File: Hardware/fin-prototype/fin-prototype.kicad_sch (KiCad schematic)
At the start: 80 parts, among them J1 USB_C_Receptacle_USB2.0_16P, J10 Conn_01x01_Pin, J11 Conn_01x01_Pin, J12 Conn_01x01_Pin, J13 Conn_01x01_Pin, J14 Conn_01x01_Pin, J15 Conn_01x01_Pin, J16 Conn_01x01_Pin, J17 Conn_01x01_Pin, J18 Conn_01x01_Pin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

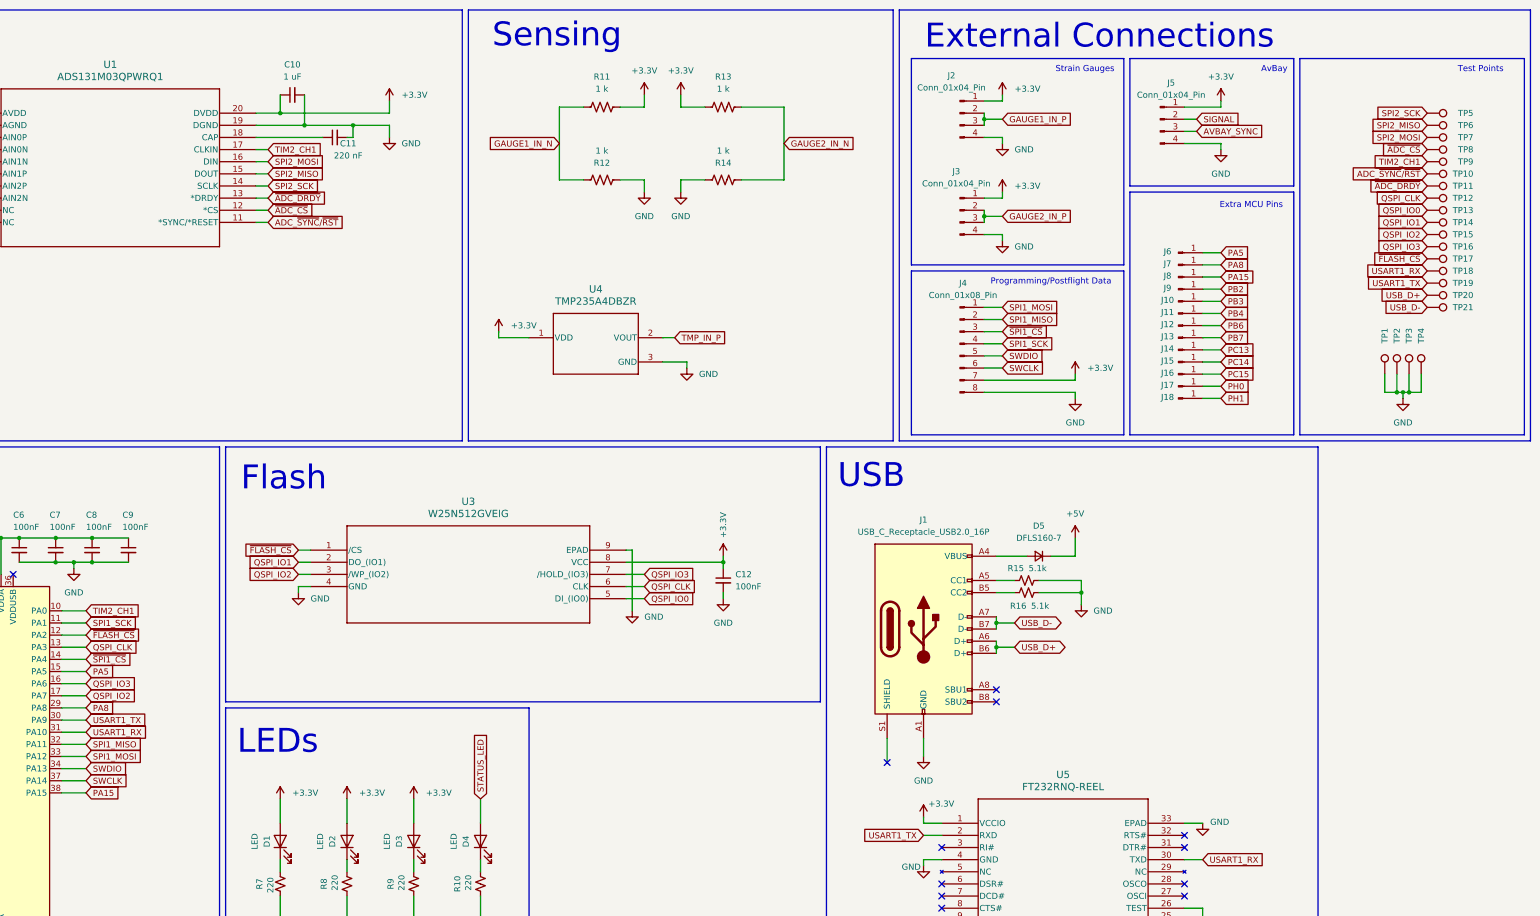
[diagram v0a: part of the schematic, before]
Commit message: place more components and silkscreen
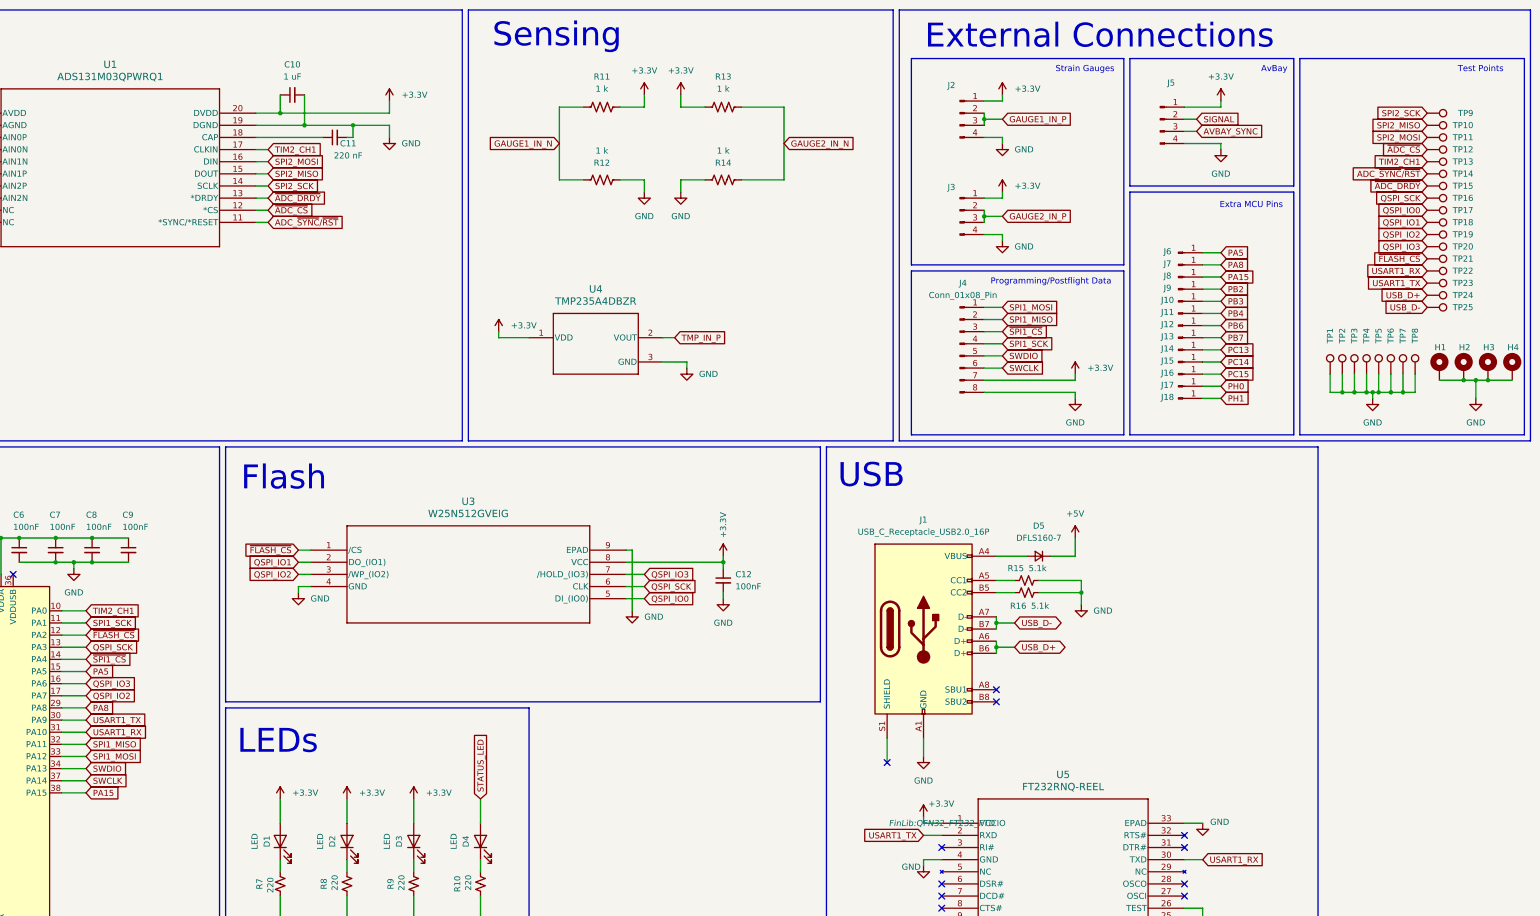
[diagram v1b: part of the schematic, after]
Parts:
- added H1, H2, H3, H4: MountingHole_Pad, MountingHole:MountingHole_2.2mm_M2_Pad, symbol Mechanical:MountingHole_Pad
- added TP5, TP6, TP7, TP8: TestPoint, Connector_PinSocket_2.54mm:PinSocket_1x01_P2.54mm_Vertical, symbol Connector:TestPoint
- D1: Signal (none) -> PWR
- D2: Signal (none) -> TX
- D3: Signal (none) -> RX
- D4: Signal (none) -> STATUS
- J10: footprint Connector_PinHeader_2.54mm:PinHeader_1x01_P2.54mm_Vertical -> FinLib:SimpleThroughHole; MCU Pin (none) -> PB3
- J11: footprint Connector_PinHeader_2.54mm:PinHeader_1x01_P2.54mm_Vertical -> FinLib:SimpleThroughHole; MCU Pin (none) -> PB4
- J12: footprint Connector_PinHeader_2.54mm:PinHeader_1x01_P2.54mm_Vertical -> FinLib:SimpleThroughHole; MCU Pin (none) -> PB6
- J13: footprint Connector_PinHeader_2.54mm:PinHeader_1x01_P2.54mm_Vertical -> FinLib:SimpleThroughHole; MCU Pin (none) -> PB7
- J14: footprint Connector_PinHeader_2.54mm:PinHeader_1x01_P2.54mm_Vertical -> FinLib:SimpleThroughHole; MCU Pin (none) -> PC13
- J15: footprint Connector_PinHeader_2.54mm:PinHeader_1x01_P2.54mm_Vertical -> FinLib:SimpleThroughHole; MCU Pin (none) -> PC14
- J16: footprint Connector_PinHeader_2.54mm:PinHeader_1x01_P2.54mm_Vertical -> FinLib:SimpleThroughHole; MCU Pin (none) -> PC15
- J17: footprint Connector_PinHeader_2.54mm:PinHeader_1x01_P2.54mm_Vertical -> FinLib:SimpleThroughHole; MCU Pin (none) -> PH0
- J18: footprint Connector_PinHeader_2.54mm:PinHeader_1x01_P2.54mm_Vertical -> FinLib:SimpleThroughHole; MCU Pin (none) -> PH1
- J2: ADC Channel (none) -> CH2
- J3: ADC Channel (none) -> CH1
- J6: footprint Connector_PinHeader_2.54mm:PinHeader_1x01_P2.54mm_Vertical -> FinLib:SimpleThroughHole; MCU Pin (none) -> PA5
- J7: footprint Connector_PinHeader_2.54mm:PinHeader_1x01_P2.54mm_Vertical -> FinLib:SimpleThroughHole; MCU Pin (none) -> PA8
- J8: footprint Connector_PinHeader_2.54mm:PinHeader_1x01_P2.54mm_Vertical -> FinLib:SimpleThroughHole; MCU Pin (none) -> PA15
- J9: footprint Connector_PinHeader_2.54mm:PinHeader_1x01_P2.54mm_Vertical -> FinLib:SimpleThroughHole; MCU Pin (none) -> PB2
- TP1, TP2, TP3, TP4: footprint TestPoint:TestPoint_Loop_D1.80mm_Drill1.0mm_Beaded -> Connector_PinHeader_2.54mm:PinHeader_1x01_P2.54mm_Vertical
- TP10: renamed from TP6; Signal (none) -> MISO
- TP11: renamed from TP7; Signal (none) -> MOSI
- TP12: renamed from TP8; Signal (none) -> CS
- TP13: renamed from TP9; Signal (none) -> CLK
- TP14: renamed from TP10; Signal (none) -> RST
- TP15: renamed from TP11; Signal (none) -> DRDY
- TP16: renamed from TP12; Signal (none) -> SCK
- TP17: renamed from TP13; Signal (none) -> IO0
- TP18: renamed from TP14; Signal (none) -> IO1
- TP19: renamed from TP15; Signal (none) -> IO2
- TP20: renamed from TP16; Signal (none) -> IO3
- TP22: renamed from TP18; Signal (none) -> RX
- TP23: renamed from TP19; Signal (none) -> TX
- TP24: renamed from TP20; Signal (none) -> USB+
- TP25: renamed from TP21; Signal (none) -> USB-
- TP9: renamed from TP5; Signal (none) -> SCK
- renumbered TP17 to TP21
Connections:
- net GND: now also H1.1, H2.1, H3.1, H4.1, TP5.1, TP6.1, TP7.1, TP8.1
- net QSPI_CLK renamed QSPI_SCK
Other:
- moved on the sheet: TP1, TP2, TP3, TP4

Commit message: Revert "place more components and silkscreen"
This reverts commit 1bc8328d4b62153ca3fb5bb472924e08519ee507.
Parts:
- removed H1, H2, H3, H4: MountingHole_Pad, MountingHole:MountingHole_2.2mm_M2_Pad, symbol Mechanical:MountingHole_Pad
- removed TP5, TP6, TP7, TP8: TestPoint, Connector_PinSocket_2.54mm:PinSocket_1x01_P2.54mm_Vertical, symbol Connector:TestPoint
- D1: Signal PWR -> (none)
- D2: Signal TX -> (none)
- D3: Signal RX -> (none)
- D4: Signal STATUS -> (none)
- J10: footprint FinLib:SimpleThroughHole -> Connector_PinHeader_2.54mm:PinHeader_1x01_P2.54mm_Vertical; MCU Pin PB3 -> (none)
- J11: footprint FinLib:SimpleThroughHole -> Connector_PinHeader_2.54mm:PinHeader_1x01_P2.54mm_Vertical; MCU Pin PB4 -> (none)
- J12: footprint FinLib:SimpleThroughHole -> Connector_PinHeader_2.54mm:PinHeader_1x01_P2.54mm_Vertical; MCU Pin PB6 -> (none)
- J13: footprint FinLib:SimpleThroughHole -> Connector_PinHeader_2.54mm:PinHeader_1x01_P2.54mm_Vertical; MCU Pin PB7 -> (none)
- J14: footprint FinLib:SimpleThroughHole -> Connector_PinHeader_2.54mm:PinHeader_1x01_P2.54mm_Vertical; MCU Pin PC13 -> (none)
- J15: footprint FinLib:SimpleThroughHole -> Connector_PinHeader_2.54mm:PinHeader_1x01_P2.54mm_Vertical; MCU Pin PC14 -> (none)
- J16: footprint FinLib:SimpleThroughHole -> Connector_PinHeader_2.54mm:PinHeader_1x01_P2.54mm_Vertical; MCU Pin PC15 -> (none)
- J17: footprint FinLib:SimpleThroughHole -> Connector_PinHeader_2.54mm:PinHeader_1x01_P2.54mm_Vertical; MCU Pin PH0 -> (none)
- J18: footprint FinLib:SimpleThroughHole -> Connector_PinHeader_2.54mm:PinHeader_1x01_P2.54mm_Vertical; MCU Pin PH1 -> (none)
- J2: ADC Channel CH2 -> (none)
- J3: ADC Channel CH1 -> (none)
- J6: footprint FinLib:SimpleThroughHole -> Connector_PinHeader_2.54mm:PinHeader_1x01_P2.54mm_Vertical; MCU Pin PA5 -> (none)
- J7: footprint FinLib:SimpleThroughHole -> Connector_PinHeader_2.54mm:PinHeader_1x01_P2.54mm_Vertical; MCU Pin PA8 -> (none)
- J8: footprint FinLib:SimpleThroughHole -> Connector_PinHeader_2.54mm:PinHeader_1x01_P2.54mm_Vertical; MCU Pin PA15 -> (none)
- J9: footprint FinLib:SimpleThroughHole -> Connector_PinHeader_2.54mm:PinHeader_1x01_P2.54mm_Vertical; MCU Pin PB2 -> (none)
- TP1, TP2, TP3, TP4: footprint Connector_PinHeader_2.54mm:PinHeader_1x01_P2.54mm_Vertical -> TestPoint:TestPoint_Loop_D1.80mm_Drill1.0mm_Beaded
- TP10: renamed from TP14; Signal RST -> (none)
- TP11: renamed from TP15; Signal DRDY -> (none)
- TP12: renamed from TP16; Signal SCK -> (none)
- TP13: renamed from TP17; Signal IO0 -> (none)
- TP14: renamed from TP18; Signal IO1 -> (none)
- TP15: renamed from TP19; Signal IO2 -> (none)
- TP16: renamed from TP20; Signal IO3 -> (none)
- TP18: renamed from TP22; Signal RX -> (none)
- TP19: renamed from TP23; Signal TX -> (none)
- TP20: renamed from TP24; Signal USB+ -> (none)
- TP21: renamed from TP25; Signal USB- -> (none)
- TP5: renamed from TP9; Signal SCK -> (none)
- TP6: renamed from TP10; Signal MISO -> (none)
- TP7: renamed from TP11; Signal MOSI -> (none)
- TP8: renamed from TP12; Signal CS -> (none)
- TP9: renamed from TP13; Signal CLK -> (none)
- renumbered TP21 to TP17
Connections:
- net QSPI_SCK renamed QSPI_CLK
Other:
- moved on the sheet: TP1, TP2, TP3, TP4
